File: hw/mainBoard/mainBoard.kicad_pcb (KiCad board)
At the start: 4 copper layers, 50 x 85 mm, 46 parts, among them IC1 ATA6561-GAQW-N, J1 LED strip, J2 G17C0900132EU, J3 JTAG, J4 G17C0900132EU, J5 Relays_board, J6 Display, J7 POWER SUPLY, J8 Conn_02x16_Odd_Even, Q3 NMOS, Q4 NMOS, SW1 SW_Push, SW2 SW_Push, U1 ESP32-WROOM-E, U3 TXU0101DBVR, U4 TLV76133DCYR, U6 LM5148RGYR

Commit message: more steps to the finale
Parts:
- moved R20 14.8 mm to (78.2, 104.1), turned to 0 degrees
- moved R18 13.8 mm to (78.2, 95.4)
- moved Rt1 9.46 mm to (78.2, 93.2)
- moved C8 6.45 mm to (83.3, 101.1)
- moved R15 4.51 mm to (78.2, 97.6)
- moved R16 4.51 mm to (78.2, 99.7)
- moved R19 4.31 mm to (78.2, 101.9)
- moved C9 1.93 mm to (88.9, 101.1)
- moved C16 1.93 mm to (86.1, 101.1)
- moved R14 1.52 mm to (78.2, 91.0)
- moved U6 1.02 mm to (85.9, 93.7)
- moved F6 0.25 mm to (71.4, 67.1)
- turned C17 to 180 degrees
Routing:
- net /Connectors/EN: track 0.00 -> 95.6 mm, vias 0 -> 1
- net /Connectors/5.2V: track 3.54 -> 89.3 mm, vias 0 -> 6
- net (no net): track 0.00 -> 79.0 mm, vias 0 -> 7
- net GND: track 0.00 -> 74.7 mm, vias 0 -> 29
- net Net-(F5-Pad2): track 0.00 -> 57.0 mm
- net /Connectors/IO36: track 0.00 -> 51.8 mm, vias 0 -> 1
- net /Connectors/IO39: track 0.00 -> 45.9 mm, vias 0 -> 1
- net Net-(IC1-CANH): track 0.00 -> 41.3 mm
- net Net-(IC1-CANL): track 21.0 -> 61.2 mm
- net /ESP32 Module/3V3: track 3.28 -> 43.3 mm, vias 0 -> 6
- net /Connectors/MOSI: track 0.00 -> 36.6 mm, vias 0 -> 1
- net /Connectors/SDA: track 0.00 -> 25.7 mm, vias 0 -> 1
- net /Connectors/SCL: track 0.00 -> 22.5 mm, vias 0 -> 1
- net /Connectors/24V: track 0.00 -> 22.1 mm, vias 0 -> 5
- net /Connectors/UART0_TX: track 0.00 -> 20.4 mm, vias 0 -> 1
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- added copper zone on In2.Cu, net /Connectors/24V
- added copper zone on In2.Cu, net /Connectors/5.2V
- added copper zone on In2.Cu, net /ESP32 Module/3V3
- added copper zone on In1.Cu, net GND
- added copper zone on In2.Cu, net GND
- added copper zone on In2.Cu, net Net-(F5-Pad2)

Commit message: lot of hw
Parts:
- moved R18 3.38 mm to (81.4, 94.2), turned to 90 degrees
- moved Q4 0.38 mm to (81.0, 84.8), turned to 0 degrees
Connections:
- U1 pad 17: (no net) -> unconnected-(U1-NC-Pad17)
- U1 pad 18: (no net) -> unconnected-(U1-NC-Pad18)
- U1 pad 19: (no net) -> unconnected-(U1-NC-Pad19)
- U1 pad 20: (no net) -> unconnected-(U1-NC-Pad20)
- U1 pad 21: (no net) -> unconnected-(U1-NC-Pad21)
- U1 pad 22: (no net) -> unconnected-(U1-NC-Pad22)
- U1 pad 32: (no net) -> unconnected-(U1-NC-Pad32)
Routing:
- net /Connectors/LED_STRIP: track 9.56 -> 111.8 mm, vias 1 -> 3
- net /Connectors/MTDO: track 5.76 -> 106.3 mm
- net /ESP32 Module/3V3: track 43.3 -> 138.6 mm, vias 6 -> 13
- net /Connectors/MTMS: track 7.66 -> 102.5 mm, vias 1 -> 2
- net /Connectors/SCL: track 22.5 -> 115.3 mm, vias 1 -> 3
- net /Connectors/IO0: track 11.5 -> 100.8 mm, vias 1 -> 2
- net /Connectors/SDA: track 25.7 -> 114.3 mm, vias 1 -> 3
- net /Connectors/MTDI: track 5.89 -> 90.9 mm, vias 1 -> 3
- net /Connectors/MTCK: track 14.0 -> 94.4 mm, vias 1 -> 2
- net (no net): track 79.0 -> 0.00 mm, vias 7 -> 0
- net /Connectors/IO16: track 8.41 -> 75.7 mm, vias 1 -> 3
- net Net-(F5-Pad2): track 57.0 -> 0.00 mm
- net Net-(U6B-SW): track 2.94 -> 53.3 mm, vias 0 -> 2
- net Net-(F6-Pad2): track 0.00 -> 44.3 mm
- net /Connectors/IO35: track 15.3 -> 58.3 mm
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- added copper zone on F.Cu, net /Connectors/24V
- added copper zone on F.Cu, net /ESP32 Module/3V3
- added copper zone on F.Cu, net Net-(U6B-SW)

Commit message: buck vedle
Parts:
- removed Q3: NMOS, NMOS-CSD18534:DQJ8
- added C15: 47uF, Capacitor_SMD:C_1210_3225Metric_Pad1.33x2.70mm_HandSolder, F.Cu at (224.0, 97.8)
- added C18: 47uF, Capacitor_SMD:C_1210_3225Metric_Pad1.33x2.70mm_HandSolder, F.Cu at (224.0, 84.8)
- added C19: 47uF, Capacitor_SMD:C_1210_3225Metric_Pad1.33x2.70mm_HandSolder, F.Cu at (224.0, 81.5)
- added C20: 10uF, Capacitor_SMD:C_1210_3225Metric_Pad1.33x2.70mm_HandSolder, F.Cu at (206.2, 95.5)
- added C21: 10uF, Capacitor_SMD:C_1210_3225Metric_Pad1.33x2.70mm_HandSolder, F.Cu at (207.4, 88.3)
- added C22: 470nF, Capacitor_SMD:C_0805_2012Metric_Pad1.18x1.45mm_HandSolder, F.Cu at (203.4, 89.6)
- added C23: 0.01uF, Capacitor_SMD:C_0805_2012Metric_Pad1.18x1.45mm_HandSolder, F.Cu at (214.4, 102.0)
- added C24: 0.01uF, Capacitor_SMD:C_0805_2012Metric_Pad1.18x1.45mm_HandSolder, F.Cu at (212.3, 102.0)
- added C25: 0.01uF, Capacitor_SMD:C_0805_2012Metric_Pad1.18x1.45mm_HandSolder, F.Cu at (210.3, 102.0)
- added C26: 0.01uF, Capacitor_SMD:C_0805_2012Metric_Pad1.18x1.45mm_HandSolder, F.Cu at (208.3, 102.0)
- added C27: 22p, Capacitor_SMD:C_0805_2012Metric_Pad1.18x1.45mm_HandSolder, F.Cu at (193.3, 96.9)
- added NT1: NetTie_2, NetTie:NetTie-2_SMD_Pad0.5mm, F.Cu at (194.5, 88.6)
- added NT1: NetTie_2, NetTie:NetTie-2_SMD_Pad0.5mm, F.Cu at (198.0, 91.7)
- added Q1: NMOS, NMOS-CSD18514:DQJ0008A, F.Cu at (212.0, 95.5)
- added R3: 10k, Resistor_SMD:R_0805_2012Metric_Pad1.20x1.40mm_HandSolder, F.Cu at (192.3, 93.8)
- C10, C17: footprint Capacitor_SMD:C_1206_3216Metric_Pad1.33x1.80mm_HandSolder -> Capacitor_SMD:C_0805_2012Metric_Pad1.18x1.45mm_HandSolder
- C16: value 2.2uF -> 4.7uF; footprint Capacitor_SMD:C_1206_3216Metric_Pad1.33x1.80mm_HandSolder -> Capacitor_SMD:C_0805_2012Metric_Pad1.18x1.45mm_HandSolder
- C8: value 10uF -> 47uF; footprint Capacitor_SMD:C_1206_3216Metric_Pad1.33x1.80mm_HandSolder -> Capacitor_SMD:C_1210_3225Metric_Pad1.33x2.70mm_HandSolder
- C9: value 4.7uF -> 2.7nF; footprint Capacitor_SMD:C_1206_3216Metric_Pad1.33x1.80mm_HandSolder -> Capacitor_SMD:C_0805_2012Metric_Pad1.18x1.45mm_HandSolder
- R14: value 40.2k -> 41.2k
- R20: footprint Resistor_SMD:R_0805_2012Metric_Pad1.20x1.40mm_HandSolder -> Resistor_SMD:R_0815_2038Metric_Pad1.20x4.05mm_HandSolder
- moved R20 150.2 mm to (227.8, 91.2), turned to 180 degrees
- moved C8 140.7 mm to (224.0, 101.1), turned to 180 degrees
- moved L2 135.4 mm to (220.2, 91.2), turned to 180 degrees
- moved Q4 131.0 mm to (212.0, 88.2), turned to -90 degrees
- moved R19 126.1 mm to (203.4, 86.3), turned to 90 degrees
- moved R15 120.1 mm to (198.3, 94.0), turned to 0 degrees
- moved R16 119.1 mm to (197.3, 97.1), turned to 90 degrees
- moved C16 116.6 mm to (202.4, 92.5), turned to 0 degrees
- moved R14 114.1 mm to (192.3, 89.9)
- moved Rt1 114.0 mm to (192.3, 91.9)
- moved R18 114.0 mm to (195.4, 94.9)
- moved U6 112.0 mm to (197.7, 89.1), turned to 90 degrees
- moved C10 109.3 mm to (201.1, 96.0), turned to -90 degrees
- moved C17 109.3 mm to (200.6, 85.5), turned to 0 degrees
- moved C9 102.5 mm to (191.3, 96.9)
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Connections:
- C10 pad 2: GND -> GNDA
- C9 pad 1: /Connectors/24V -> Net-(C9-Pad1)
- C9 pad 2: GND -> GNDA
- R14 pad 1: GND -> GNDA
- R15 pad 2: GND -> GNDA
- Rt1 pad 2: GND -> GNDA
- U6 pad 1: unconnected-(U6B-NC-Pad1) -> GND
- U6 pad 22: unconnected-(U6B-NC-Pad22) -> GND
- U6 pad 23: unconnected-(U6B-NC-Pad23) -> GND
- U6 pad 24: unconnected-(U6B-NC-Pad24) -> GND
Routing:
- net Net-(U6B-SW): track 53.3 -> 8.37 mm
- net /Connectors/24V: track 51.5 -> 8.35 mm, vias 5 -> 2
- net /Power Suply/ISNS+: track 43.0 -> 0.00 mm
- net /ESP32 Module/3V3: track 138.6 -> 109.4 mm, vias 13 -> 11
- net /Power Suply/LM_POWER_GOOD: track 30.1 -> 7.95 mm
- net /Connectors/5.2V: track 50.4 -> 29.3 mm, vias 10 -> 5
- net GND: track 83.5 -> 67.3 mm, vias 43 -> 46
- net Net-(U6A-LO): track 17.4 -> 1.23 mm, vias 2 -> 1
- net /Connectors/MTMS: track 102.5 -> 86.7 mm
- net /Connectors/SCL: track 115.3 -> 131.0 mm
- net /Connectors/SDA: track 114.3 -> 129.8 mm
- net /Connectors/MTDI: track 90.9 -> 75.6 mm, vias 3 -> 2
- net /Connectors/LED_STRIP: track 111.8 -> 98.3 mm, vias 3 -> 2
- net /Connectors/MTCK: track 94.4 -> 82.0 mm
- net /Connectors/MTDO: track 106.3 -> 96.1 mm
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- added copper zone on F.Cu, net /Connectors/5.2V
- added copper zone on F.Cu, net /Power Suply/ISNS+
- added copper zone on F.Cu, net GNDA
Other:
- board size 50 x 85 mm -> 122.3 x 85 mm

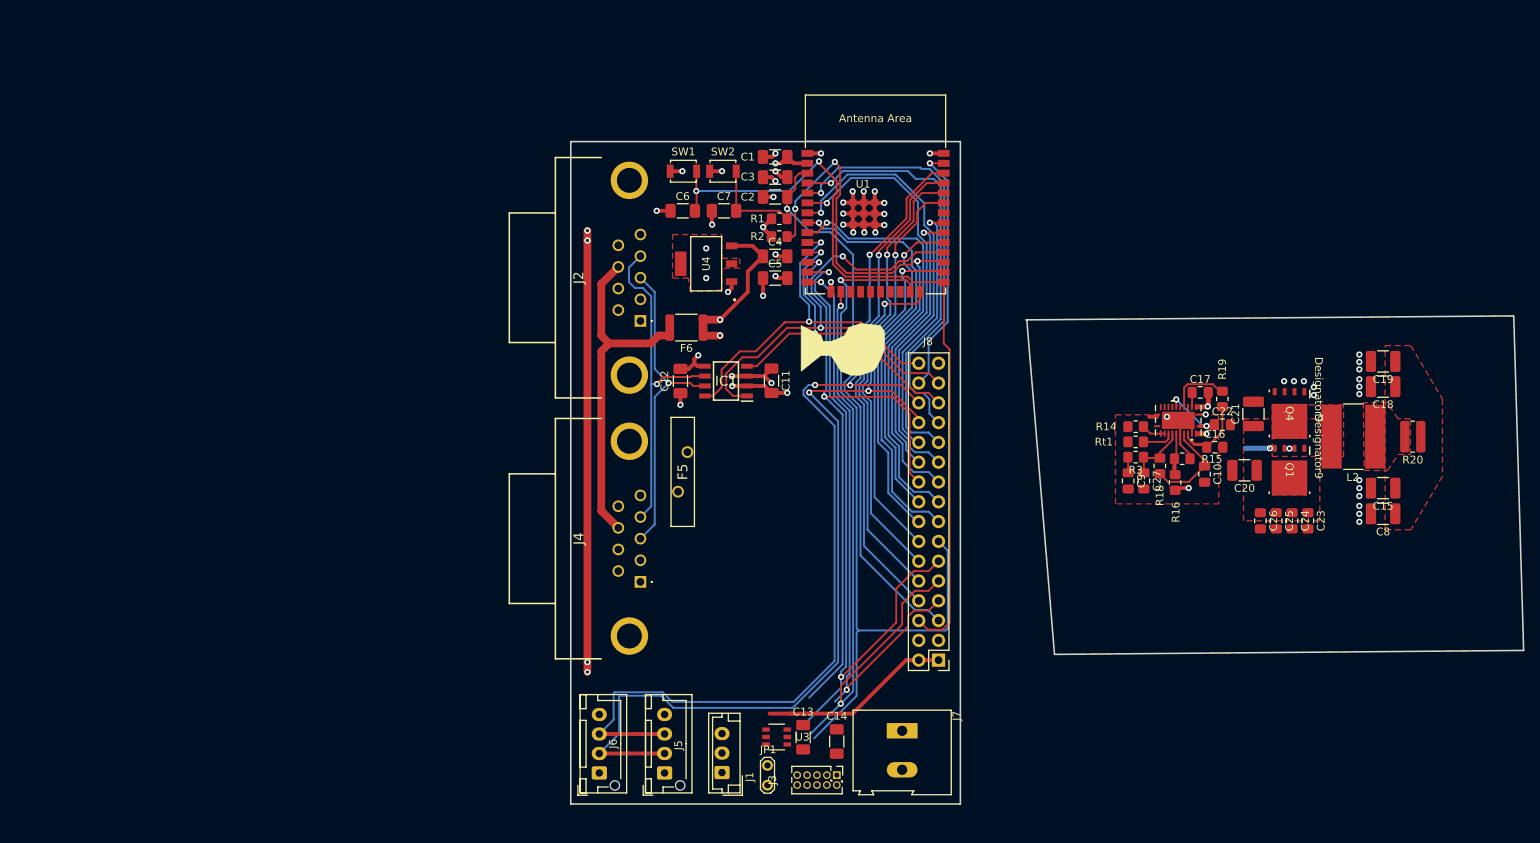
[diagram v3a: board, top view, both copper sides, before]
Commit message: hotovo bez silkscreenu
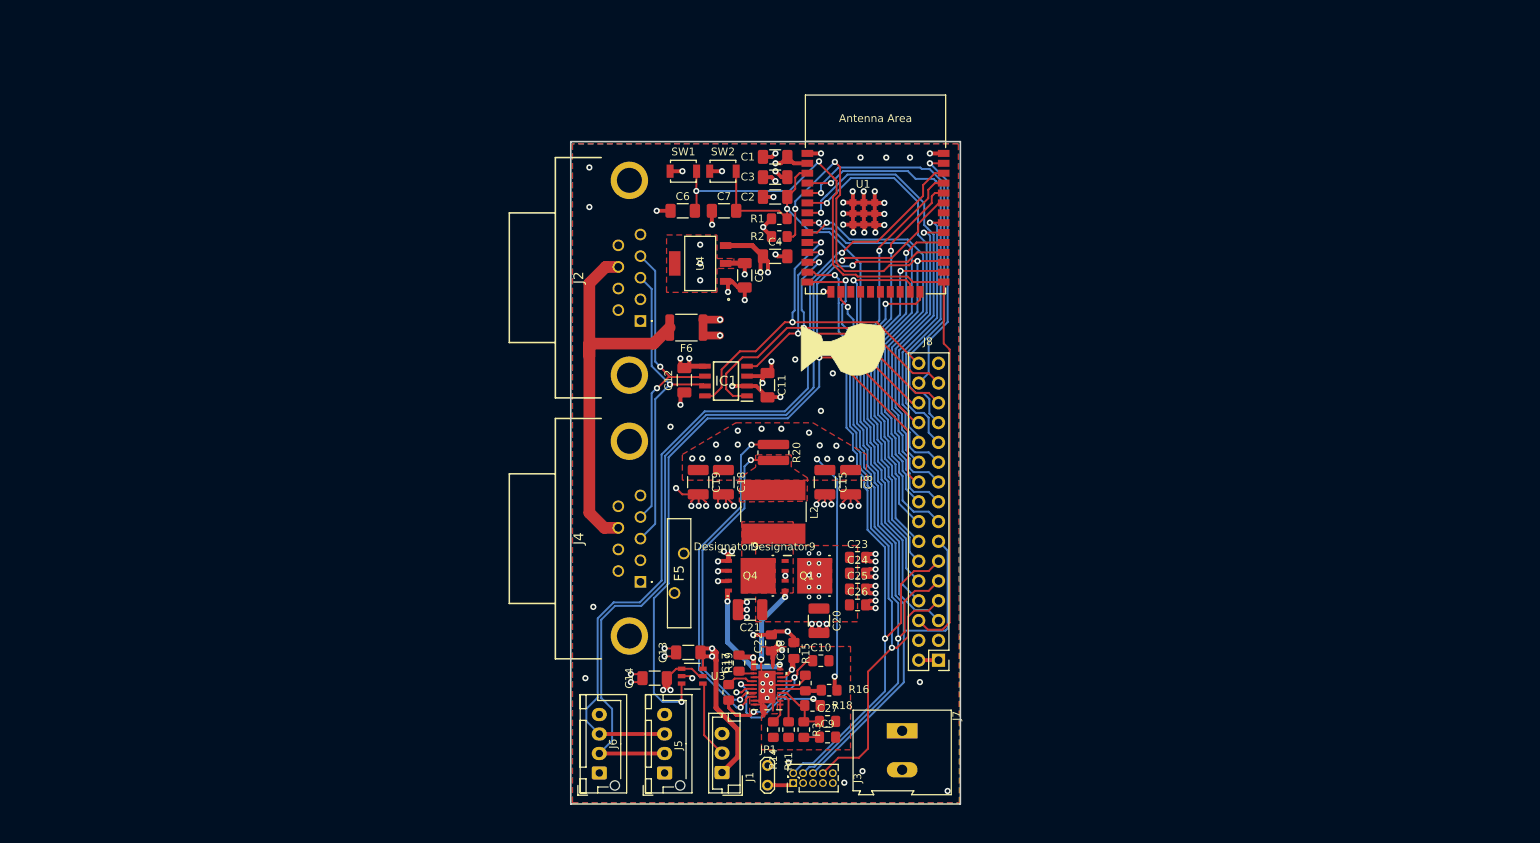
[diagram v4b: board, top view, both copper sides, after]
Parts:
- moved C19 89.2 mm to (136.1, 97.0), turned to -90 degrees
- moved C18 85.5 mm to (139.4, 97.0), turned to -90 degrees
- moved R20 82.1 mm to (145.8, 93.2), turned to -90 degrees
- moved L2 75.0 mm to (145.8, 100.8), turned to -90 degrees
- moved R19 73.7 mm to (140.1, 124.0)
- moved Q4 72.3 mm to (142.8, 109.0), turned to 0 degrees
- moved C15 71.6 mm to (152.4, 97.0), turned to -90 degrees
- moved C21 69.3 mm to (142.8, 113.4), turned to 180 degrees
- moved C17 68.6 mm to (141.4, 120.2), turned to 90 degrees
- moved C8 68.4 mm to (155.7, 97.0), turned to -90 degrees
- moved C22 64.3 mm to (145.5, 117.7), turned to 90 degrees
- moved Q1 63.4 mm to (150.1, 109.0), turned to 0 degrees
- moved U6 62.9 mm to (145.0, 123.3), turned to 180 degrees
- moved NT1 62.7 mm to (144.5, 126.5), turned to 90 degrees
- moved R14 60.6 mm to (145.8, 128.8), turned to 90 degrees
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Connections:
- Q4 pad 3: unconnected-(Q4-S-Pad3) -> GND
- U6 pad 2: unconnected-(U6B-NC-Pad2) -> Net-(U6A-CNFG)
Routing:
- net /Connectors/5.2V: track 29.3 -> 122.1 mm, vias 5 -> 27
- net GND: track 67.3 -> 152.1 mm, vias 46 -> 89
- net /Power Suply/ISNS+: track 0.00 -> 41.1 mm, vias 0 -> 2
- net /Connectors/24V: track 8.35 -> 26.9 mm, vias 2 -> 13
- net /Connectors/LED_STRIP: track 98.3 -> 114.4 mm, vias 2 -> 3
- net Net-(U6A-LO): track 1.23 -> 15.1 mm, vias 1 -> 2
- net /Power Suply/VDDA: track 12.3 -> 25.6 mm, vias 0 -> 3
- net /ESP32 Module/3V3: track 109.4 -> 96.7 mm
- net /Connectors/MTDI: track 75.6 -> 86.6 mm
- net Net-(J1-Pin_2): track 0.00 -> 9.94 mm
- net Net-(U6B-VCC): track 9.49 -> 18.3 mm, vias 0 -> 2
- net Net-(U6B-SW): track 8.37 -> 15.4 mm
- net Net-(F6-Pad2): track 44.3 -> 51.4 mm
- net Net-(U6A-HO): track 4.59 -> 10.9 mm
- net /Power Suply/LM_POWER_GOOD: track 7.95 -> 3.68 mm
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- added copper zone on B.Cu, net GND
- added copper zone on F.Cu, net GND
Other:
- board size 122.3 x 85 mm -> 50 x 85 mm

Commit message: finale bez rybicky
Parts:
- added REF**: ESD-Logo_6.6x6mm_SilkScreen, Symbol:ESD-Logo_6.6x6mm_SilkScreen, F.Cu at (138.1, 90.1)
- added REF**: MountingHole_2.2mm_M2_Pad, MountingHole:MountingHole_2.2mm_M2_Pad, F.Cu at (166.6, 137.9)
- added REF**: OSHW-Logo2_7.3x6mm_SilkScreen, Symbol:OSHW-Logo2_7.3x6mm_SilkScreen, F.Cu at (154.1, 102.7)
- added REF**: MountingHole_2.2mm_M2_Pad, MountingHole:MountingHole_2.2mm_M2_Pad, F.Cu at (125.0, 50.5)
- added SJ1: SolderJumper-2_P1.3mm_Open_RoundedPad1.0x1.5mm, Jumper:SolderJumper-2_P1.3mm_Open_RoundedPad1.0x1.5mm, F.Cu at (142.2, 66.6)
- L1: renamed from L2; value 2.7uH -> 3.6uH
- R3: renamed from R20; value 25m -> 10m
- Rt1: value 9.1k -> 35.7k
- moved J7 2.19 mm to (162.3, 126.7)
- renumbered SW1 to BOOT, C6 to C1, C18 to C10, C19 to C11, C24 to C12, C25 to C13, C23 to C14, C21 to C15, C8 to C16, C15 to C17, C26 to C18, C13 to C19, C7 to C2, C14 to C20, C22 to C21, C17 to C22, C10 to C23, C16 to C24, C27 to C25, C20 to C26, C9 to C27, C1 to C4, C2 to C5, C12 to C6, C11 to C7, C5 to C8, C4 to C9, F6 to F1, F5 to F2, J2 to J1, J4 to J2, J6 to J3, J1 to J4, J3 to J6, NT1 to NT2, Q4 to Q2, R14 to R4, R3 to R5, R19 to R6, R15 to R7, R16 to R8, R18 to R9, SW2 to RST, U4 to U2, U6 to U4
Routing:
- net /ESP32 Module/3V3: track 96.7 -> 95.0 mm
- net /Connectors/5.2V: track 122.1 -> 120.7 mm
- net GND: track 152.1 -> 151.4 mm, vias 89 -> 98
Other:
- board size 50 x 85 mm -> 50 x 94.2 mm
- board text added: "+3V3 from board"
- board text added: "10"
- board text added: "11"
- board text added: "12"
- board text added: "13"
- board text added: "14"
- board text added: "15"
- board text added: "16"
- board text added: "17"
- board text added: "18"
- board text added: "19"
- board text added: "20"
- board text added: "2024 Jakub Charvot, FEKT VUT"
- board text added: "21"
- board text added: "22"
- board text added: "23"
- board text added: "24"
- board text added: "25"
- board text added: "26"
- board text added: "27"
- board text added: "28"
- board text added: "29"
- board text added: "30"
- board text added: "31"
- board text added: "32"
- board text added: "3V3"
- board text added: "5"
- board text added: "6"
- board text added: "7"
- board text added: "8"
- board text added: "9"
- board text added: "Aqua Control"
- board text added: "Display"
- board text added: "JTAG"
- board text added: "LED strip"
- board text added: "MAIN PCB - v1.0"
- board text added: "Relays"
